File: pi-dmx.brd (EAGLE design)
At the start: 85.1 x 56.1 mm, 32 parts, among them IC4 74HCT08D, Q1 MMBTA56-SOT23, Q2 BCW71SMD, X1 MSTBV2, X2 NC3FBH2, X3 NC3MBH

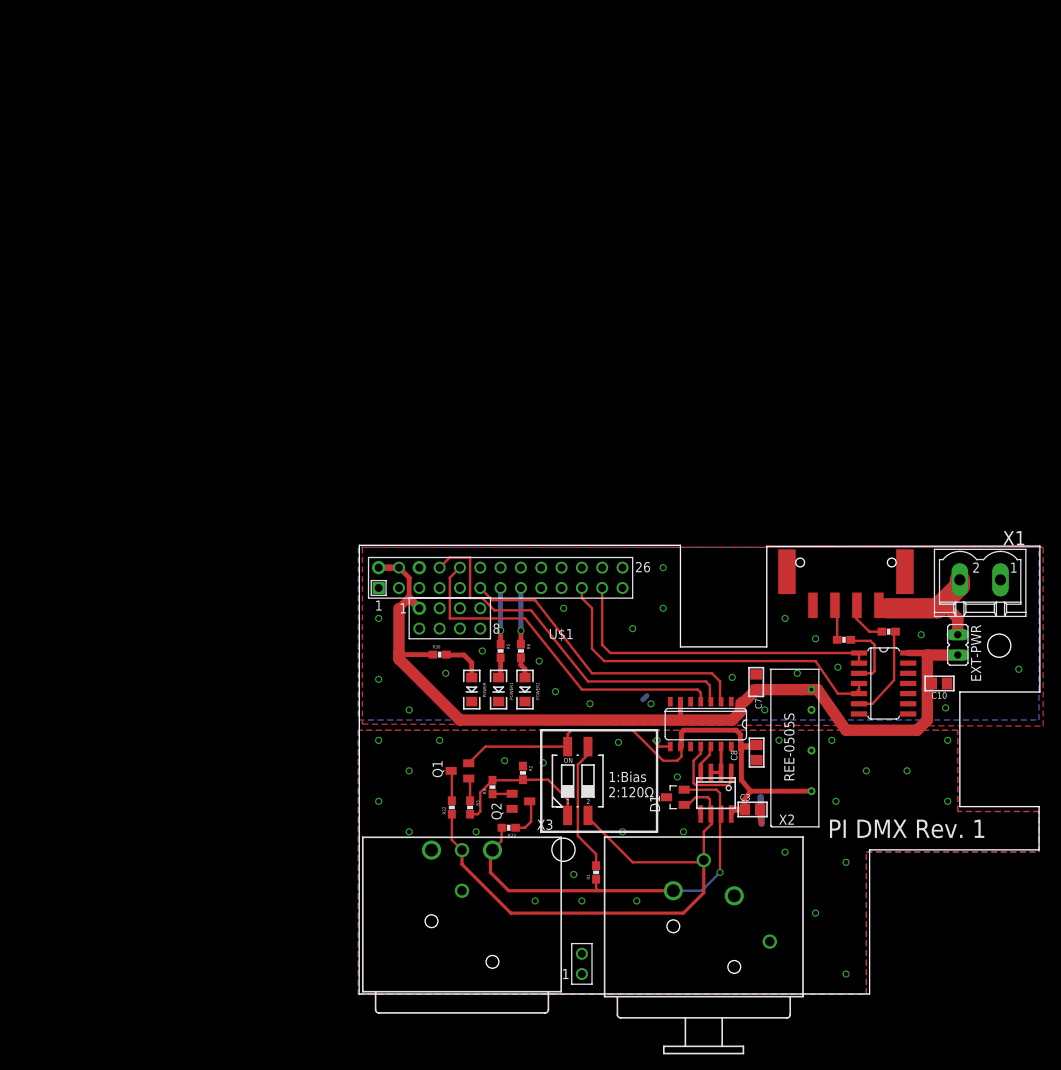
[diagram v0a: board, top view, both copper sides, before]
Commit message: Labels cleaned up
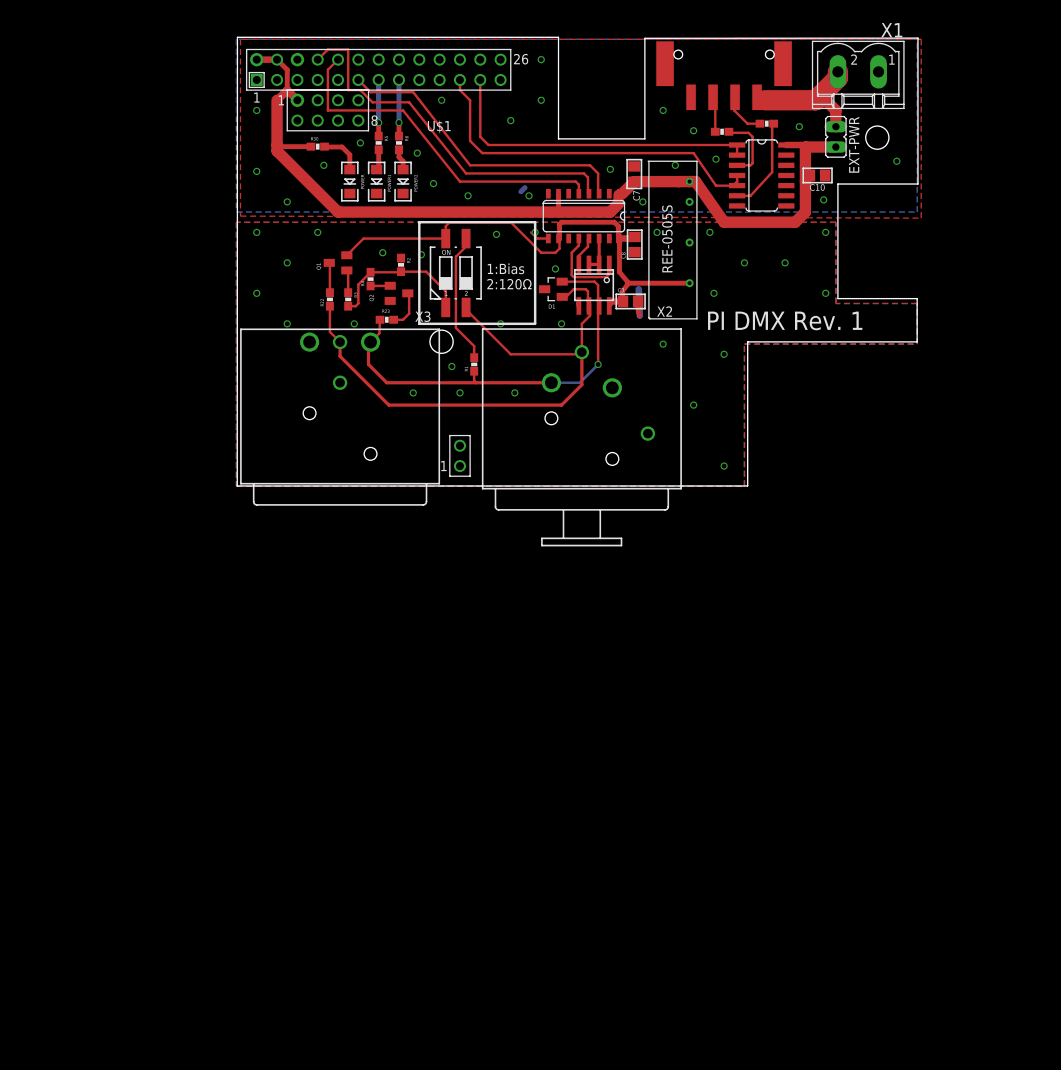
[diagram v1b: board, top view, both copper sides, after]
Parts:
- moved C10 65.3 mm to (72.6, 38.9)
- moved C3 65.3 mm to (49.3, 23.1)
- moved C7 65.3 mm to (49.7, 39.0)
- moved C8 65.3 mm to (49.8, 30.2)
- moved D1 65.3 mm to (39.6, 24.6)
- moved EXT-PWR 65.3 mm to (74.9, 43.7)
- moved IC4 65.3 mm to (65.7, 38.9)
- moved POWER 65.3 mm to (14.2, 38.1)
- moved POWER1 65.3 mm to (17.5, 38.1)
- moved POWER2 65.3 mm to (20.8, 38.1)
- moved Q1 65.3 mm to (12.7, 27.9)
- moved Q2 65.3 mm to (20.3, 24.1)
- moved R1 65.3 mm to (29.7, 15.2)
- moved R2 65.3 mm to (20.6, 27.7)
- moved R22 65.3 mm to (11.7, 23.4)
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
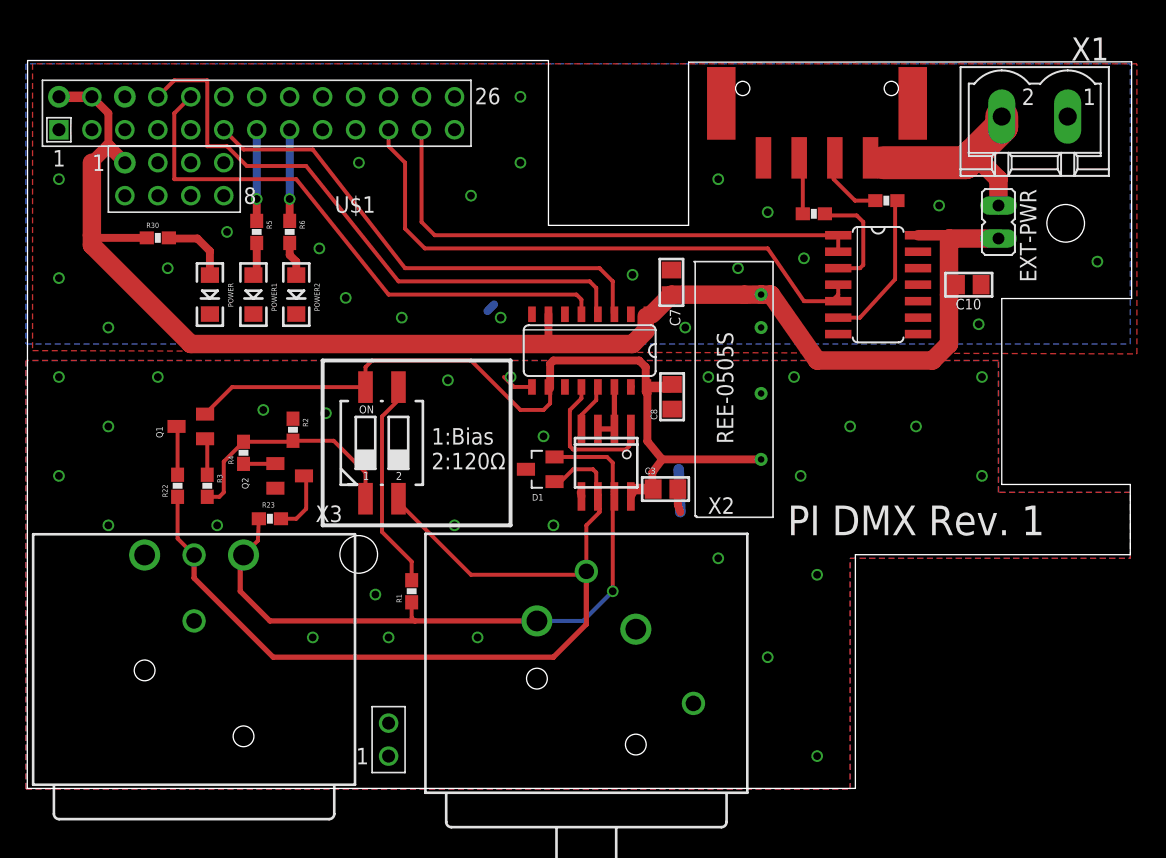
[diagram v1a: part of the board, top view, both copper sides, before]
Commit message: Added reset button and fixed connector layout
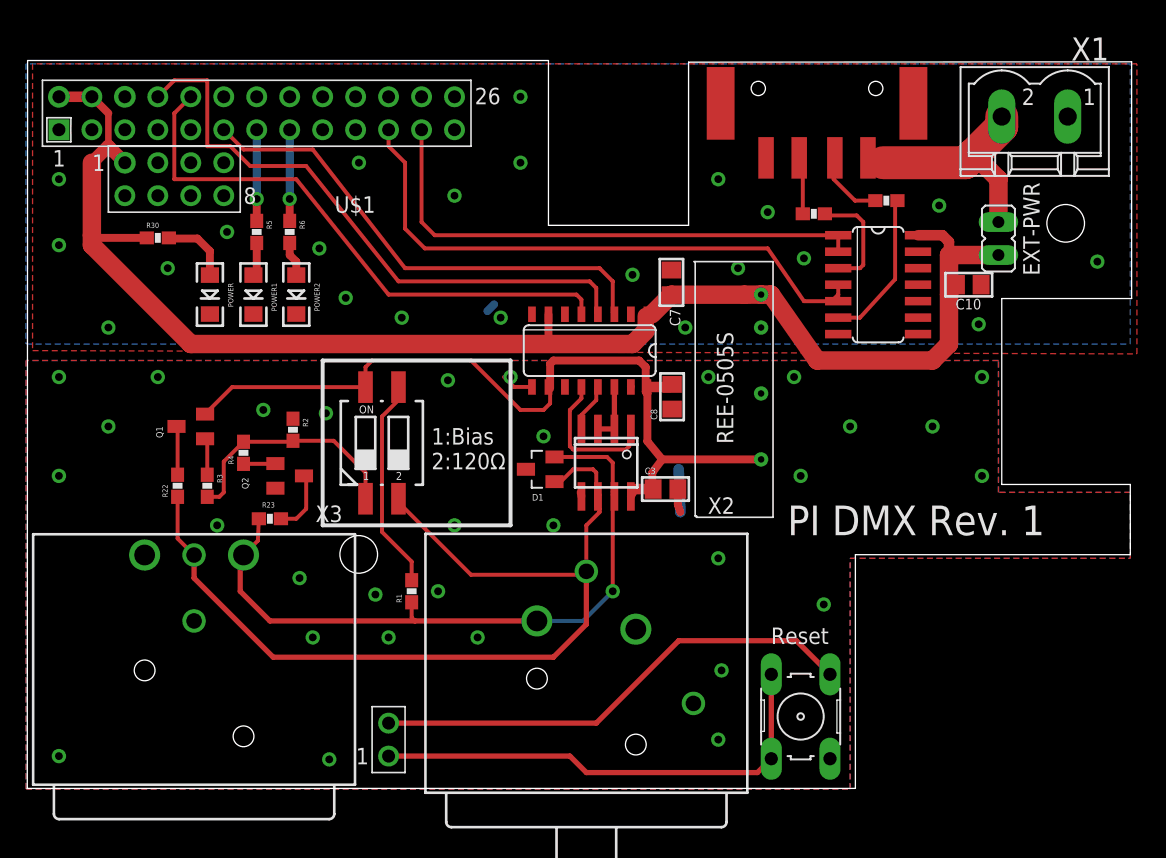
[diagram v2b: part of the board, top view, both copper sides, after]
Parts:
- added S2: (no value), switch-omron:B3F-10XX
- moved EXT-PWR 1.27 mm to (74.9, 42.4)
- renumbered U$11 to U$2
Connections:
- removed net RESET: U$1.P6_1
- new net N$11: S2.3, S2.4, U$1.P6_1
- net GND: now also S2.1, S2.2
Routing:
- net GND: track 0.72 -> 38.4 mm
- net N$11: track 0.00 -> 37.0 mm
- net N$10: track 16.9 -> 18.4 mm
- net VCC: track 120.2 -> 119.7 mm
- net GND1: vias 28 -> 31
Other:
- board text added: "Reset"

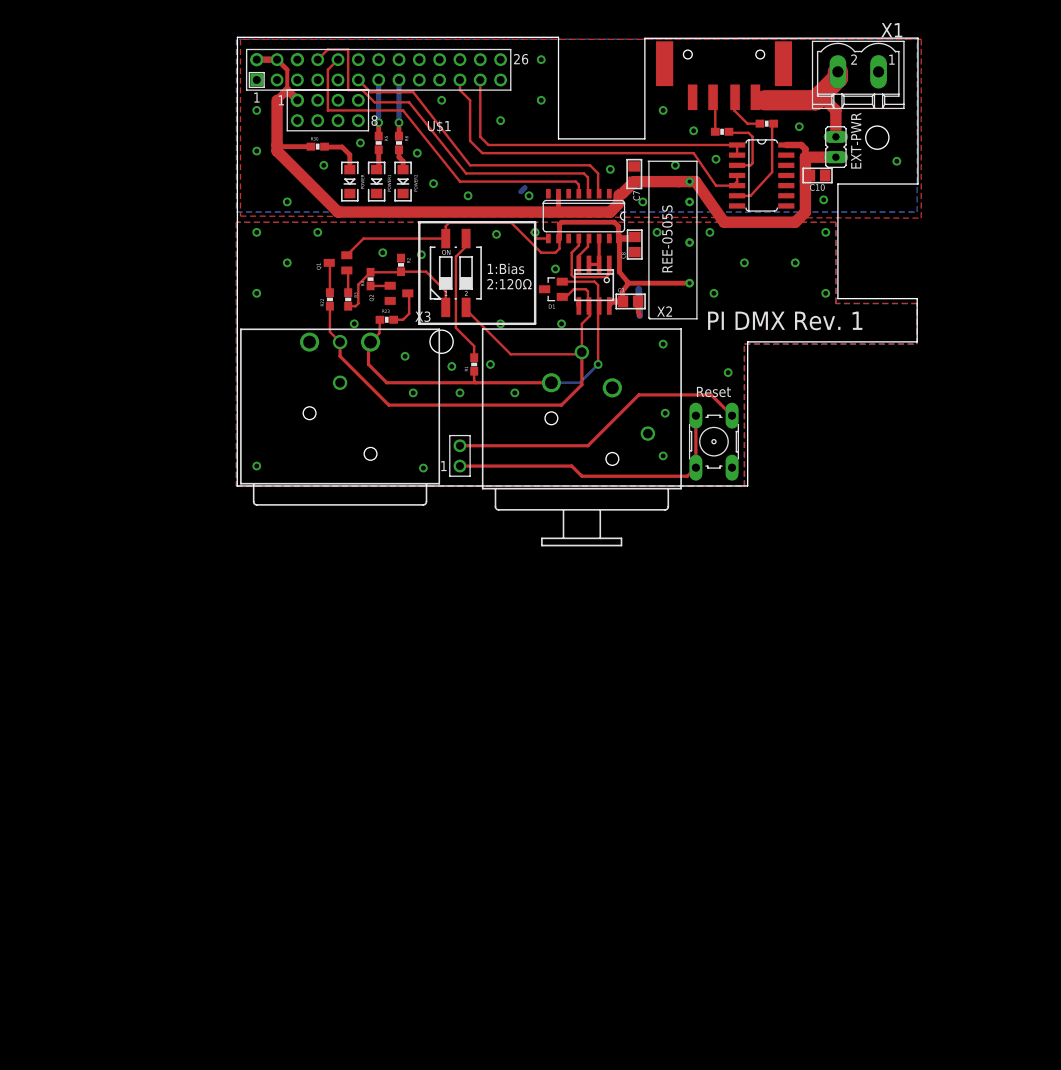
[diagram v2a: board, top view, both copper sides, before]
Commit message: Raspberry Pi 3 version
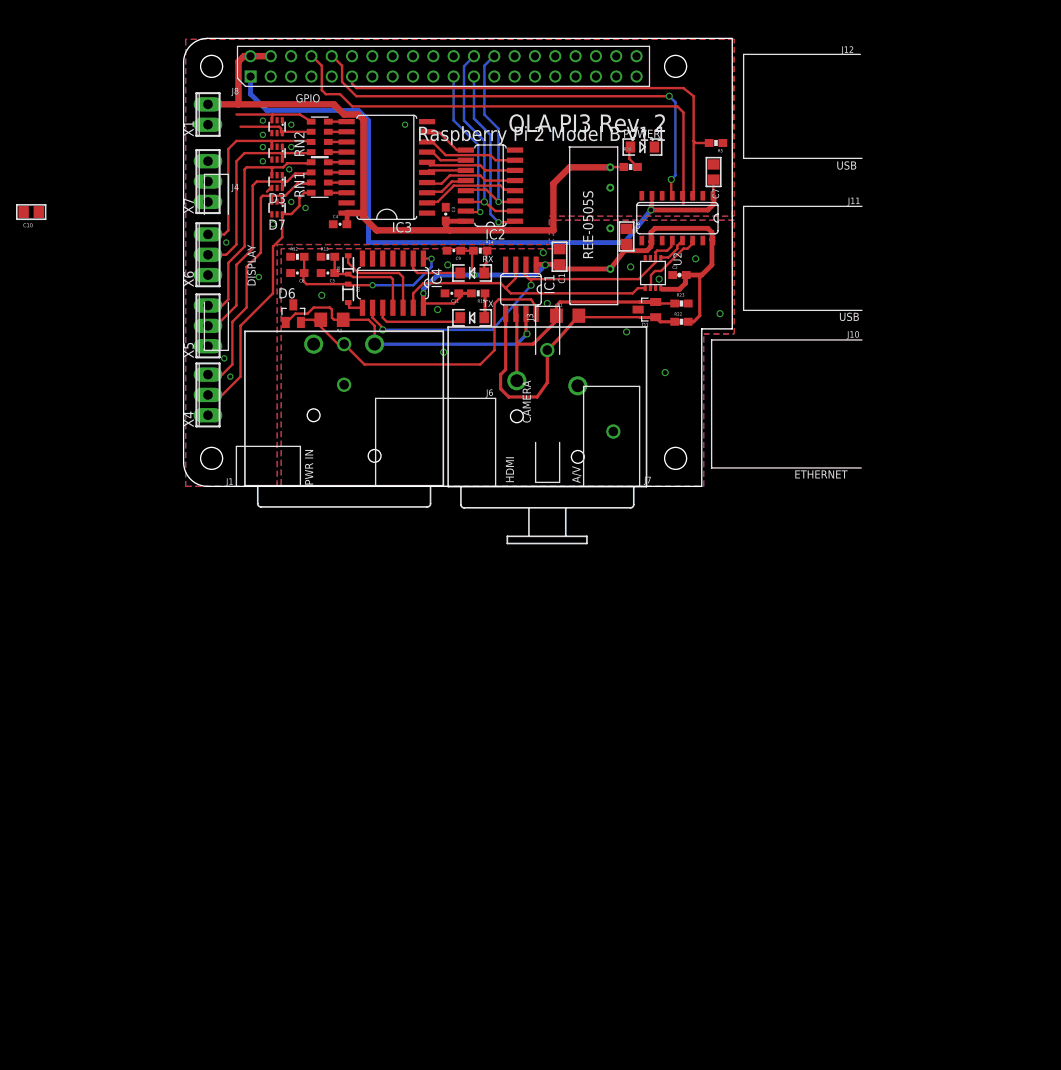
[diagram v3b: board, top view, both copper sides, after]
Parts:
- removed EXT-PWR: (no value), jumper:JP1
- removed POWER1, POWER2: (no value), SparkFun-LED:LED-1206
- removed Q1: MMBTA56-SOT23, transistor-pnp:SOT23
- removed Q2: BCW71SMD, transistor-npn:SOT23-BEC
- removed R24, R27: 100R, SparkFun-Passives:0603-RES
- removed R3, R4: 10K, SparkFun-Passives:0603-RES
- removed R6: 330R, SparkFun-Passives:0603-RES
- removed S1: 219-02, switch-dil:CTS-219-02
- removed S2: (no value), switch-omron:B3F-10XX
- removed U$1: RPI-B-V2SHIELD, raspberry:RPI-B-V2-SHIELD
- removed U$2: 1778780, grant:1778780
- removed U$7: MAX485SO8, hartmodems:SO8
- added C1: 1uF, microbuilder:0805
- added C11, C4, C9: 0.1uF, SparkFun-Capacitors:0603-CAP
- added C2: 0.1uF, SparkFun-Passives:0603-CAP
- added C5, C6: 10N, SparkFun-Capacitors:0603-CAP
- added D2, D8: 250mA/100V, SparkFun-DiscreteSemi:SOD-323
- added D3, D4, D5, D7: MMBZ5221BS_MMBZ5259BS, m-pad-2.1:SOT363_PHILIPS
- added D6: PESD1CAN, diode:SOT23
- added IC1: MAX488CSA, maxim:SO08
- added IC2: 74AC139D, 74xx-eu:SO16
- added IC3: 74HC540DW, 74xx-eu:SO20W
- added PCB1: RPI2, e14_Rpi2_RevA:RPI2
- added R12, R13: 1M, SparkFun-Resistors:0603-RES
- added R14, R15: 330R, SparkFun-Resistors:0603-RES
- added RN1, RN2: 100R, resistor-dil:EXBS8V
- added RX, TX: (no value), SparkFun-LED:LED-1206
- added U2: SN74LVC2G157-DCT, m-pad-2.1:SSOP8
- added X4: STRIP1, con-phoenix-254:3POL254
- added X5: STRIP2, con-phoenix-254:3POL254
- added X6: STRIP3, con-phoenix-254:3POL254
- added X7: STRIP4, con-phoenix-254:3POL254
- C3: value 1uF -> 0.1uF; device microbuilder:0805 -> SparkFun-Capacitors:0603-CAP
- IC4: value 74HCT08D -> 74HC14D; device logic:SO14 -> 74xx-eu:SO14
- R1: device SparkFun-Passives:0603-RES -> SparkFun-Resistors:1206
- R2: value 10K -> 120R; device SparkFun-Passives:0603-RES -> SparkFun-Resistors:1206
- R5: value 330R -> 10K
- X1: value MSTBV2 -> 5V; device con-phoenix-508:MSTBV2 -> con-phoenix-254:2POL254
- moved C10 98.4 mm to (-25.7, 34.3)
- moved X1 81.5 mm to (-3.56, 46.5), turned to 90 degrees
- moved IC4 48.0 mm to (19.6, 25.4), turned to 180 degrees
- moved R22 44.0 mm to (55.6, 20.6), turned to 0 degrees
- moved R5 42.2 mm to (59.9, 42.9), turned to 180 degrees
- moved R30 39.2 mm to (49.3, 39.9)
- moved R23 36.9 mm to (55.6, 22.9)
- moved POWER 36.8 mm to (50.7, 42.4), turned to 0 degrees
- moved C3 25.6 mm to (26.2, 34.0), turned to 270 degrees
- moved R1 13.2 mm to (41.4, 21.3), turned to 0 degrees
- moved D1 12.0 mm to (51.3, 22.1)
- moved U$8 11.7 mm to (55.1, 33.5)
- moved R2 11.0 mm to (11.9, 20.8), turned to 180 degrees
- moved U$6 10.1 mm to (41.7, 42.4)
- moved C7 9.91 mm to (59.6, 39.3)
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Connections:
- removed net EMISO: R27.2, U$2.2
- removed net ESCLK: R24.2, U$2.3
- removed net GPIO30: U$1.P5_5
- removed net GPIO31: U$1.P5_6
- removed net I2C0_SCL/GPIO29: U$1.P5_4
- removed net I2C0_SDA/GPIO28: U$1.P5_3
- removed net N$89: IC4.3, R24.1
- new net CE0: IC2.14, IC2.2, PCB1.P$24
- new net CE1: IC2.13, IC2.3, PCB1.P$26
- new net MISO0: D7.3, RN1.7, X4.3
- new net MISO1: D3.3, RN1.5, X5.3
- new net MISO2: D5.3, RN2.7, X6.3
- new net MISO3: D4.3, RN2.5, X7.3
- new net N$12: IC3.15, RN1.4
- new net N$13: IC2.4, IC3.2
- new net N$14: IC2.5, IC3.4
- new net N$15: IC2.6, IC3.6
- new net N$16: IC2.7, IC3.8
- new net N$17: IC2.12, IC3.3
- new net N$18: IC2.11, IC3.5
- new net N$20: IC2.9, IC3.9
- new net N$21: C6.1, D2.C, IC4.1, R12.2
- new net N$27: IC4.10, TX.C
- new net N$32: IC3.14, RN2.1
- new net N$33: IC3.13, RN2.2
- new net N$34: IC3.12, RN2.3
- new net N$35: IC3.11, RN2.4
- new net SCLK0: D7.6, RN1.8, X4.2
- new net SCLK1: D3.6, RN1.6, X5.2
- new net SCLK2: D5.6, RN2.8, X6.2
- new net SCLK3: D4.6, RN2.6, X7.2
- net +3V3: now also C7.2, PCB1.P$1, U$8.1, U$8.7; no longer U$1.P1_1, U$1.P1_17, U$1.P5_2
- net 5V: now also C1.2, C11.1, C2.2, C9.1, IC1.1, IC4.14, R14.2, R15.2, R22.2, U2.8; no longer C3.2, Q1.2, S1.4, U$7.8
- net DIRECTION: now also PCB1.P$11, R5.2; no longer U$1.P1_11
- net GND: now also C3.1, C4.1, D3.1, D3.4, D4.1, D4.4, D5.1, D5.4, D7.1, D7.4, IC2.8, IC3.1, IC3.10, IC3.19, PCB1.P$14, PCB1.P$25, PCB1.P$30, PCB1.P$39, PCB1.P$6, PCB1.P$9, R5.1, X4.1, X5.1, X6.1, X7.1; no longer IC4.7, POWER1.C, POWER2.C, S2.1, S2.2, U$1.P1_14, U$1.P1_20, U$1.P1_25, U$1.P1_6, U$1.P1_9, U$1.P5_7, U$1.P5_8, U$1.P6_2, U$2.4
- net GND1: now also C1.1, C11.2, C2.1, C5.2, C6.2, C9.2, D6.3, IC1.4, IC4.7, R12.1, R13.1, R23.1, U2.4, U2.7; no longer C3.1, Q2.E, U$7.5
- net MISO: now also IC2.15, PCB1.P$21; no longer IC4.4, IC4.5, U$1.P1_21
- net N$1: now also D2.A, IC4.8; no longer R5.1, U$1.P1_13
- net N$10: now also C5.1, D8.C, IC4.11, R13.2; no longer EXT-PWR.1, U$2.1, X1.2
- net N$11: now also IC3.16, RN1.3; no longer S2.3, S2.4, U$1.P6_1
- net N$19: now also IC2.10, IC3.7; no longer IC4.6, R27.1
- net N$2: now also D8.A, IC4.12; no longer POWER1.A, R5.2
- net N$22: now also IC1.5, R1.2; no longer S1.2, U$7.6, X3.3
- net N$23: now also IC1.6; no longer U$7.7, X3.2
- net N$24: now also R14.1, RX.A; no longer U$7.4, U$8.13
- net N$25: now also IC4.2, RX.C; no longer Q1.3, R22.2
- net N$26: now also R15.1, TX.A; no longer Q2.C, R23.1
- net N$28: now also IC1.2, IC4.9, U2.2; no longer U$7.1
- net N$3: now also D6.1, IC1.7, R2.1, X3.2; no longer R1.2, S1.3
- net N$4: now also U$8.14, U2.6; no longer R2.2, R3.2, R4.2, S1.1
- net N$5: now also U$8.13, U2.1; no longer U$7.2, U$7.3, U$8.14
- net N$6: now also D6.2, IC1.8, R2.2, X3.3; no longer Q1.1, R3.1
- net N$7: now also IC3.17, RN1.2; no longer Q2.B, R4.1
- net N$8: now also IC1.3, IC4.13, U2.5; no longer POWER2.A, R6.2
- net N$9: now also IC3.18, RN1.1; no longer R6.1, U$1.P1_15
- net RX: now also PCB1.P$10; no longer U$1.P1_10
- net SCLK: now also IC2.1, PCB1.P$23; no longer IC4.1, IC4.2, U$1.P1_23
- net TX: now also PCB1.P$8; no longer U$1.P1_8
- net VCC: now also C3.2, C4.2, IC2.16, IC3.20, PCB1.P$2, PCB1.P$4, X1.2; no longer C7.2, EXT-PWR.2, IC4.14, U$1.P1_2, U$1.P1_4, U$1.P5_1, U$8.1, U$8.7
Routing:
- net +3V3: track 0.00 -> 84.8 mm, vias 0 -> 1
- net N$6: track 2.84 -> 41.1 mm
- net GND: track 38.4 -> 0.81 mm, vias 22 -> 15
- net N$28: track 11.4 -> 48.4 mm, vias 0 -> 2
- net N$11: track 37.0 -> 2.28 mm
- net MISO0: track 0.00 -> 33.7 mm
- net N$22: track 75.0 -> 41.3 mm
- net N$8: track 2.69 -> 35.6 mm
- net SCLK0: track 0.00 -> 32.8 mm
- net MISO1: track 0.00 -> 29.6 mm
- net SCLK1: track 0.00 -> 29.5 mm
- net VCC: track 119.7 -> 91.2 mm
- net CE0: track 0.00 -> 26.4 mm, vias 0 -> 1
- net CE1: track 0.00 -> 26.4 mm, vias 0 -> 1
- net MISO: track 45.8 -> 20.2 mm, vias 0 -> 1
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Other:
- board size 85.1 x 56.1 mm -> 68.6 x 56 mm
- board text added: "OLA PI3 Rev. 2"
- board text removed: "1:Bias 2:120Ω"
- board text removed: "PI DMX Rev. 1"
- board text removed: "Reset"

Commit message: Board mfg candidate
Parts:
- moved C10 31.9 mm to (2.79, 48.8)
- moved X1 0.51 mm to (-3.56, 46.0)
- moved C9 0.51 mm to (27.2, 29.0)
- moved R14 0.51 mm to (30.5, 29.0)
- moved X4 0.51 mm to (-3.56, 10.9)
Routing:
- net SCLK3: track 9.47 -> 18.8 mm
- net MISO3: track 10.4 -> 16.9 mm
- net SCLK0: track 32.8 -> 35.5 mm
- net MISO0: track 33.7 -> 35.2 mm
- net SCLK1: track 29.5 -> 31.0 mm
- net N$6: track 41.1 -> 40.1 mm
- net 5V: track 79.7 -> 79.2 mm
- net GND: track 0.81 -> 0.70 mm, vias 15 -> 27
